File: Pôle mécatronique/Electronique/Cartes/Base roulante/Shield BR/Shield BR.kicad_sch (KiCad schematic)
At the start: 37 parts, among them J1 Conn_01x04_Male, J2 Conn_01x04_Female, J3 Conn_01x04_Female, J4 Conn_01x04_Female, J5 Conn_01x04_Female, J5-CAN1 Conn_01x02_Female, SW1 SW_Push_SPDT, U1 R-78E5.0-0.5, U2 MCP2551-I-P

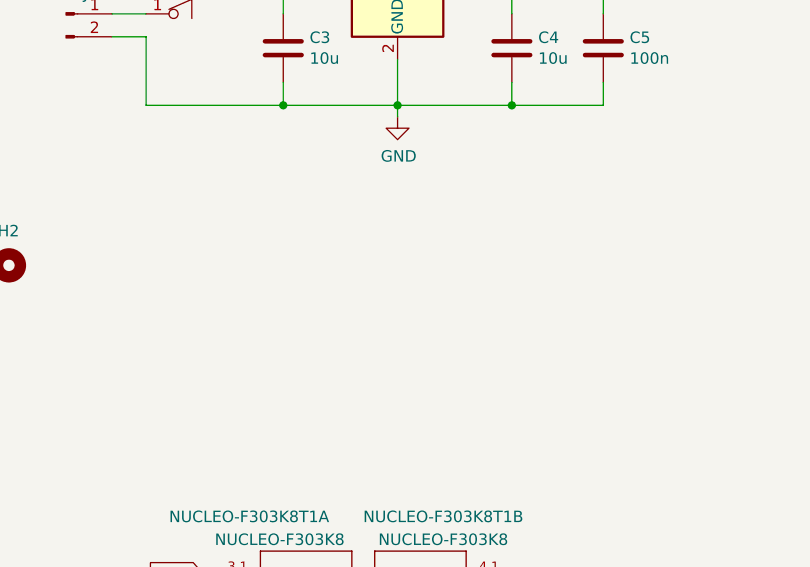
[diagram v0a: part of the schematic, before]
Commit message: Ajout points de masse
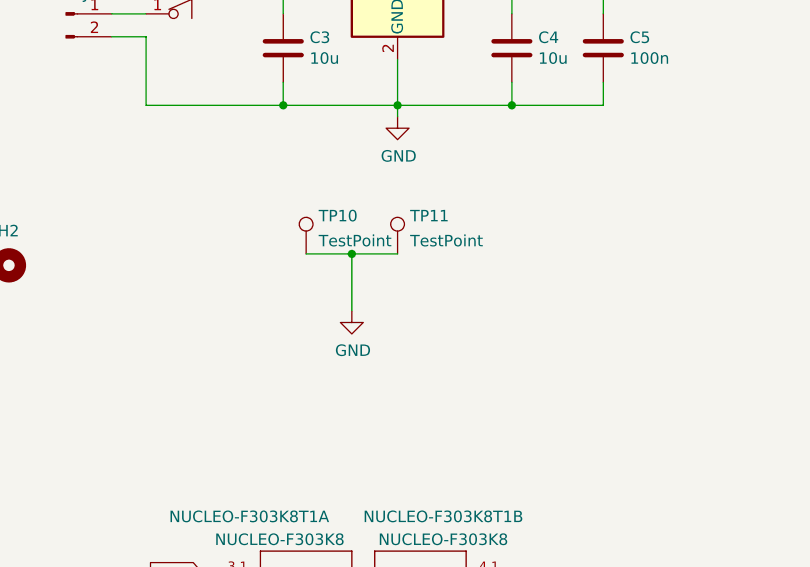
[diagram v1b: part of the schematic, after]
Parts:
- added TP10, TP11: TestPoint, TestPoint:TestPoint_Pad_D2.0mm, symbol Connector:TestPoint
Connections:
- net GND: now also TP10.1, TP11.1
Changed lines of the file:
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@@
   (junction (at 187.96 134.62) (diameter 0) (color 0 0 0 0)
+  )
+  (junction (at 88.9 62.23) (diameter 0) (color 0 0 0 0)
   )
   (junction (at 186.69 96.52) (diameter 0) (color 0 0 0 0)
@@
     (stroke (width 0) (type default) (color 0 0 0 0))
   )
+  (wire (pts (xy 83.82 62.23) (xy 88.9 62.23))
+    (stroke (width 0) (type default) (color 0 0 0 0))
+  )
   (wire (pts (xy 179.07 115.57) (xy 179.07 116.84))
     (stroke (width 0) (type default) (color 0 0 0 0))
@@
     (stroke (width 0) (type default) (color 0 0 0 0))
   )
+  (wire (pts (xy 88.9 62.23) (xy 88.9 68.58))
+    (stroke (width 0) (type default) (color 0 0 0 0))
+  )
   (wire (pts (xy 62.23 35.56) (xy 66.04 35.56))
     (stroke (width 0) (type default) (color 0 0 0 0))
@@
   )
   (wire (pts (xy 38.1 133.35) (xy 40.64 133.35))
+    (stroke (width 0) (type default) (color 0 0 0 0))
+  )
+  (wire (pts (xy 88.9 62.23) (xy 93.98 62.23))
     (stroke (width 0) (type default) (color 0 0 0 0))
   )
@@
     (pin "1")
   )
+  (symbol (lib_id "power:GND") (at 88.9 68.58 0) (unit 1)
+    (in_bom yes) (on_board yes)
+    (property "Reference" "#PWR019" (id 0) (at 88.9 74.93 0)
+      (effects (font (size 1.27 1.27)) hide)
+    )
+    (property "Value" "GND" (id 1) (at 89.027 72.9742 0))
+    (property "Footprint" "" (id 2) (at 88.9 68.58 0)
+      (effects (font (size 1.27 1.27)) hide)
+    )
+    (property "Datasheet" "" (id 3) (at 88.9 68.58 0)
+      (effects (font (size 1.27 1.27)) hide)
+    )
+    (pin "1")
+  )
   (symbol (lib_id "Device:C") (at 116.84 39.37 0) (unit 1)
     (in_bom yes) (on_board yes)
@@
     (pin "1")
   )
+  (symbol (lib_id "Connector:TestPoint") (at 83.82 62.23 0) (unit 1)
+    (in_bom yes) (on_board yes) (fields_autoplaced)
+    (property "Reference" "TP10" (id 0) (at 85.217 58.0195 0)
+      (effects (font (size 1.27 1.27)) (justify left))
+    )
+    (property "Value" "TestPoint" (id 1) (at 85.217 60.7946 0)
+      (effects (font (size 1.27 1.27)) (justify left))
+    )
+    (property "Footprint" "TestPoint:TestPoint_Pad_D2.0mm" (id 2) (at 88.9 62.23 0)
+      (effects (font (size 1.27 1.27)) hide)
+    )
+    (property "Datasheet" "~" (id 3) (at 88.9 62.23 0)
+      (effects (font (size 1.27 1.27)) hide)
+    )
+    (pin "1")
+  )
   (symbol (lib_id "Connector:TestPoint") (at 208.28 54.61 180) (unit 1)
     (in_bom yes) (on_board yes) (fields_autoplaced)
@@
     (pin "2")
   )
+  (symbol (lib_id "Connector:TestPoint") (at 93.98 62.23 0) (unit 1)
+    (in_bom yes) (on_board yes) (fields_autoplaced)
+    (property "Reference" "TP11" (id 0) (at 95.377 58.0195 0)
+      (effects (font (size 1.27 1.27)) (justify left))
+    )
+    (property "Value" "TestPoint" (id 1) (at 95.377 60.7946 0)
+      (effects (font (size 1.27 1.27)) (justify left))
+    )
+    (property "Footprint" "TestPoint:TestPoint_Pad_D2.0mm" (id 2) (at 99.06 62.23 0)
+      (effects (font (size 1.27 1.27)) hide)
+    )
+    (property "Datasheet" "~" (id 3) (at 99.06 62.23 0)
+      (effects (font (size 1.27 1.27)) hide)
+    )
+    (pin "1")
+  )
   (symbol (lib_id "Connector:TestPoint") (at 38.1 133.35 90) (unit 1)
     (in_bom yes) (on_board yes) (fields_autoplaced)
@@
       (reference "#PWR018") (unit 1) (value "GND") (footprint "")
     )
+    (path "/849ef7e5-8097-4aee-8015-323905546838"
+      (reference "#PWR019") (unit 1) (value "GND") (footprint "")
+    )
     (path "/0acb9a70-0945-4b13-8c86-e1fe36897257"
       (reference "C1") (unit 1) (value "100nF") (footprint "Capacitor_SMD:C_1206_3216Metric_Pad1.33x1.80mm_HandSolder")
@@
       (reference "TP9") (unit 1) (value "TestPoint") (footprint "TestPoint:TestPoint_Pad_D2.0mm")
     )
+    (path "/db5b3db1-1522-4f64-8767-8904a5729aa9"
+      (reference "TP10") (unit 1) (value "TestPoint") (footprint "TestPoint:TestPoint_Pad_D2.0mm")
+    )
+    (path "/fabcdf52-b758-43bb-a760-cb0bfaea8957"
+      (reference "TP11") (unit 1) (value "TestPoint") (footprint "TestPoint:TestPoint_Pad_D2.0mm")
+    )
     (path "/00000000-0000-0000-0000-00005f920486"

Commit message: Vérif JLC
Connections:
- net Dir2: now also NUCLEO-F303K8T1.4.11 (PA1); no longer NUCLEO-F303K8T1.4.12 (PA0)
- net Dir3: now also NUCLEO-F303K8T1.3.8 (PB6); no longer NUCLEO-F303K8T1.3.9 (PB1)
- net Stp2: now also NUCLEO-F303K8T1.4.10 (PA3); no longer NUCLEO-F303K8T1.4.11 (PA1)
- net Stp3: now also NUCLEO-F303K8T1.3.9 (PB1); no longer NUCLEO-F303K8T1.3.10 (PF0)
